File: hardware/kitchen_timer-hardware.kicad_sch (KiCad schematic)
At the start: 15 parts

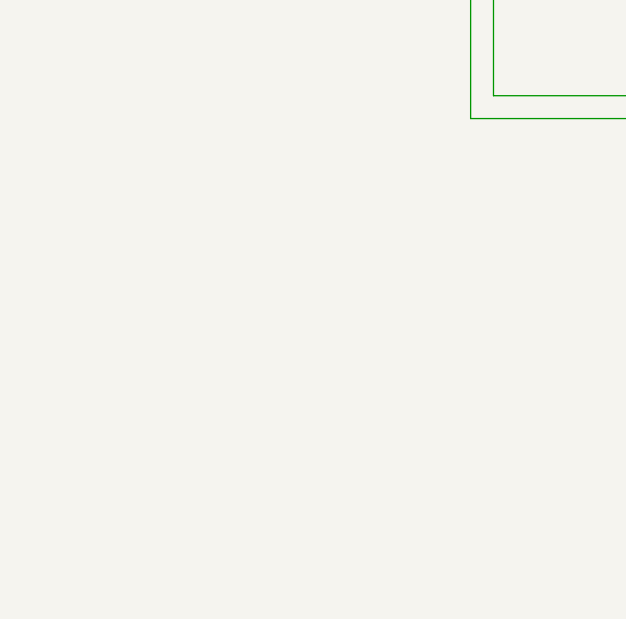
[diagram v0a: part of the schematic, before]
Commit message: Added mounting holes.
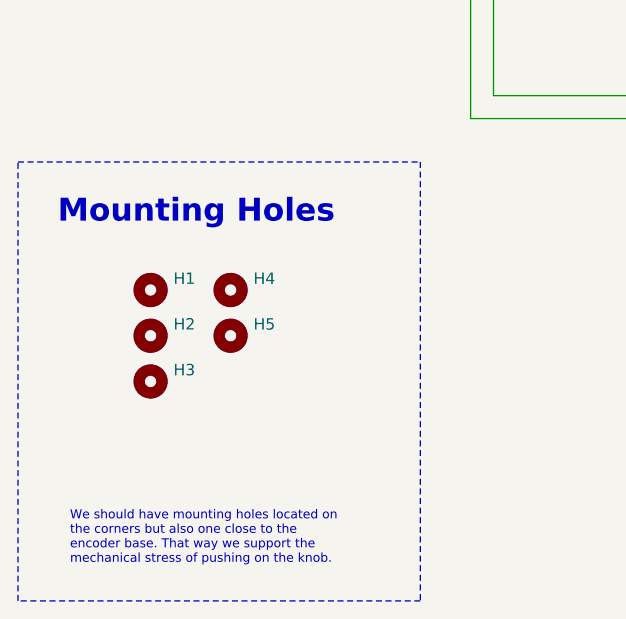
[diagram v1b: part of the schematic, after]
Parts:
- added H1, H2, H3, H4, H5: MountingHole, symbol Mechanical:MountingHole
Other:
- note added: "Mounting Holes"

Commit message: Electric Rules Check completed.
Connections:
- net ${VCC} Boost Converter/PP_GND is gone; now on net GND: TP11.1
- net BMS & Power Path/GND-USB is gone; now on net GND: TP15.1
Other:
- sheet ${VCC} Boost Converter ports: added none; removed PP_GND
- sheet BMS & Power Path ports: added GND; removed GND-USB, PP_GND
- sheet LED Matrices Display ports: added ${MAT1A}{DIG}, ${MAT1A}{SEG}, ${MAT1B}{DIG}, ${MAT1B}{SEG}, ${MAT2A}{DIG}, ${MAT2A}{SEG}, ${MAT2B}{DIG}, ${MAT2B}{SEG}; removed ${MAT1A}_DIG, ${MAT1A}_SEG, ${MAT1B}_DIG, ${MAT1B}_SEG, ${MAT2A}_DIG, ${MAT2A}_SEG, ${MAT2B}_DIG, ${MAT2B}_SEG
- sheet LED Matrices Drivers ports: added ${MAT1A}{DIG}, ${MAT1B}{DIG}, ${MAT1B}{SEG}, ${MAT2A}{DIG}, ${MAT2A}{SEG}, ${MAT2B}{DIG}, ${MAT2B}{SEG}, Mat1A{SEG}; removed ${MAT1A}_DIG, ${MAT1A}_SEG, ${MAT1B}_DIG, ${MAT1B}_SEG, ${MAT2A}_DIG, ${MAT2A}_SEG, ${MAT2B}_DIG, ${MAT2B}_SEG
- sheet USB-C & UART Debugger ports: added GND; removed GND-USB
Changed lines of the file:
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@@
 	)
 	(junction
-		(at 124.46 140.97)
-		(diameter 0)
-		(color 0 0 0 0)
-	)
-	(junction
 		(at 123.19 93.98)
 		(diameter 0)
@@
 	)
 	(junction
+		(at 124.46 140.97)
+		(diameter 0)
+		(color 0 0 0 0)
+	)
+	(junction
 		(at 123.19 88.9)
 		(diameter 0)
@@
 	(wire
 		(pts
+			(xy 124.46 140.97) (xy 128.27 140.97)
+		)
+		(stroke
+			(width 0)
+			(type default)
+		)
+	)
+	(wire
+		(pts
 			(xy 123.19 93.98) (xy 135.89 93.98)
 		)
@@
 		)
 	)
-	(wire
-		(pts
-			(xy 124.46 140.97) (xy 138.43 140.97)
-		)
-		(stroke
-			(width 0)
-			(type default)
-		)
-	)
 	(bus
 		(pts
@@
 	(wire
 		(pts
+			(xy 128.27 140.97) (xy 128.27 144.78)
+		)
+		(stroke
+			(width 0)
+			(type default)
+		)
+	)
+	(wire
+		(pts
 			(xy 55.88 68.58) (xy 55.88 67.31)
 		)
@@
 	(wire
 		(pts
-			(xy 66.04 71.12) (xy 66.04 140.97)
-		)
-		(stroke
-			(width 0)
-			(type default)
-		)
-	)
-	(wire
-		(pts
 			(xy 62.23 57.15) (xy 62.23 58.42)
 		)
@@
 	(wire
 		(pts
-			(xy 66.04 140.97) (xy 86.36 140.97)
-		)
-		(stroke
-			(width 0)
-			(type default)
-		)
-	)
-	(wire
-		(pts
-			(xy 55.88 71.12) (xy 66.04 71.12)
+			(xy 55.88 71.12) (xy 59.69 71.12)
 		)
 		(stroke
@@
 		)
 	)
+	(wire
+		(pts
+			(xy 59.69 71.12) (xy 59.69 74.93)
+		)
+		(stroke
+			(width 0)
+			(type default)
+		)
+	)
 	(bus
 		(pts
@@
 	(global_label "GND"
 		(shape output)
+		(at 59.69 74.93 0)
+		(fields_autoplaced yes)
+		(effects
+			(font
+				(size 1.27 1.27)
+			)
+			(justify left)
+		)
+		(property "Intersheetrefs" "${INTERSHEET_REFS}"
+			(at 66.5457 74.93 0)
+			(effects
+				(font
+					(size 1.27 1.27)
+				)
+				(justify left)
+				(hide yes)
+			)
+		)
+	)
+	(global_label "GND"
+		(shape output)
+		(at 128.27 144.78 0)
+		(fields_autoplaced yes)
+		(effects
+			(font
+				(size 1.27 1.27)
+			)
+			(justify left)
+		)
+		(property "Intersheetrefs" "${INTERSHEET_REFS}"
+			(at 135.1257 144.78 0)
+			(effects
+				(font
+					(size 1.27 1.27)
+				)
+				(justify left)
+				(hide yes)
+			)
+		)
+	)
+	(global_label "GND"
+		(shape output)
 		(at 186.69 140.97 0)
 		(fields_autoplaced yes)
@@
 			)
 		)
-		(pin "${MAT1A}_DIG" output
-			(at 218.44 53.34 0)
+		(pin "Mat1A{SEG}" output
+			(at 218.44 50.8 0)
 			(effects
 				(font
@@
 			)
 		)
-		(pin "${MAT1A}_SEG" output
-			(at 218.44 50.8 0)
+		(pin "${MAT1A}{DIG}" output
+			(at 218.44 53.34 0)
 			(effects
 				(font
@@
 			)
 		)
-		(pin "${MAT1B}_DIG" output
+		(pin "${MAT1B}{DIG}" output
 			(at 218.44 59.69 0)
 			(effects
@@
 			)
 		)
-		(pin "${MAT1B}_SEG" output
+		(pin "${MAT1B}{SEG}" output
 			(at 218.44 57.15 0)
 			(effects
@@
 			)
 		)
-		(pin "${MAT2A}_DIG" output
+		(pin "${MAT2A}{DIG}" output
 			(at 218.44 66.04 0)
 			(effects
@@
 			)
 		)
-		(pin "${MAT2A}_SEG" output
+		(pin "${MAT2A}{SEG}" output
 			(at 218.44 63.5 0)
 			(effects
@@
 			)
 		)
-		(pin "${MAT2B}_DIG" output
+		(pin "${MAT2B}{DIG}" output
 			(at 218.44 72.39 0)
 			(effects
@@
 			)
 		)
-		(pin "${MAT2B}_SEG" output
+		(pin "${MAT2B}{SEG}" output
 			(at 218.44 69.85 0)
 			(effects
@@
 			)
 		)
-		(pin "${MAT1A}_DIG" input
+		(pin "${MAT1A}{DIG}" input
 			(at 236.22 53.34 180)
 			(effects
@@
 			)
 		)
-		(pin "${MAT1A}_SEG" input
+		(pin "${MAT1A}{SEG}" input
 			(at 236.22 50.8 180)
 			(effects
@@
 			)
 		)
-		(pin "${MAT1B}_DIG" input
+		(pin "${MAT1B}{DIG}" input
 			(at 236.22 59.69 180)
 			(effects
@@
 			)
 		)
-		(pin "${MAT2A}_DIG" input
-			(at 236.22 66.04 180)
+		(pin "${MAT1B}{SEG}" input
+			(at 236.22 57.15 180)
 			(effects
 				(font
@@
 			)
 		)
-		(pin "${MAT2A}_SEG" input
-			(at 236.22 63.5 180)
+		(pin "${MAT2A}{DIG}" input
+			(at 236.22 66.04 180)
 			(effects
 				(font
@@
 			)
 		)
-		(pin "${MAT2B}_DIG" input
-			(at 236.22 72.39 180)
+		(pin "${MAT2A}{SEG}" input
+			(at 236.22 63.5 180)
 			(effects
 				(font
@@
 			)
 		)
-		(pin "${MAT2B}_SEG" input
-			(at 236.22 69.85 180)
+		(pin "${MAT2B}{DIG}" input
+			(at 236.22 72.39 180)
 			(effects
 				(font
@@
 			)
 		)
-		(pin "${MAT1B}_SEG" input
-			(at 236.22 57.15 180)
+		(pin "${MAT2B}{SEG}" input
+			(at 236.22 69.85 180)
 			(effects
 				(font
@@
 			)
 		)
-		(pin "PP_GND" input
-			(at 138.43 140.97 180)
-			(effects
-				(font
-					(size 1.27 1.27)
-				)
-				(justify left)
-			)
-		)
 		(pin "GND" output
 			(at 171.45 140.97 0)
@@
 			)
 		)
-		(pin "GND-USB" input
-			(at 86.36 140.97 180)
-			(effects
-				(font
-					(size 1.27 1.27)
-				)
-				(justify left)
-			)
-		)
 		(pin "+5V-USB" input
 			(at 86.36 138.43 180)
@@
 			)
 		)
-		(pin "PP_GND" output
+		(pin "GND" output
 			(at 119.38 140.97 0)
 			(effects
@@
 			)
 		)
-		(pin "GND-USB" output
-			(at 52.07 71.12 0)
+		(pin "CH340_RXD" input
+			(at 52.07 55.88 0)
 			(effects
 				(font
@@
 			)
 		)
-		(pin "CH340_RXD" input
-			(at 52.07 55.88 0)
+		(pin "­CH340_TXD" output
+			(at 52.07 53.34 0)
 			(effects
 				(font
@@
 			)
 		)
-		(pin "­CH340_TXD" output
-			(at 52.07 53.34 0)
+		(pin "GND" output
+			(at 52.07 71.12 0)
 			(effects
 				(font

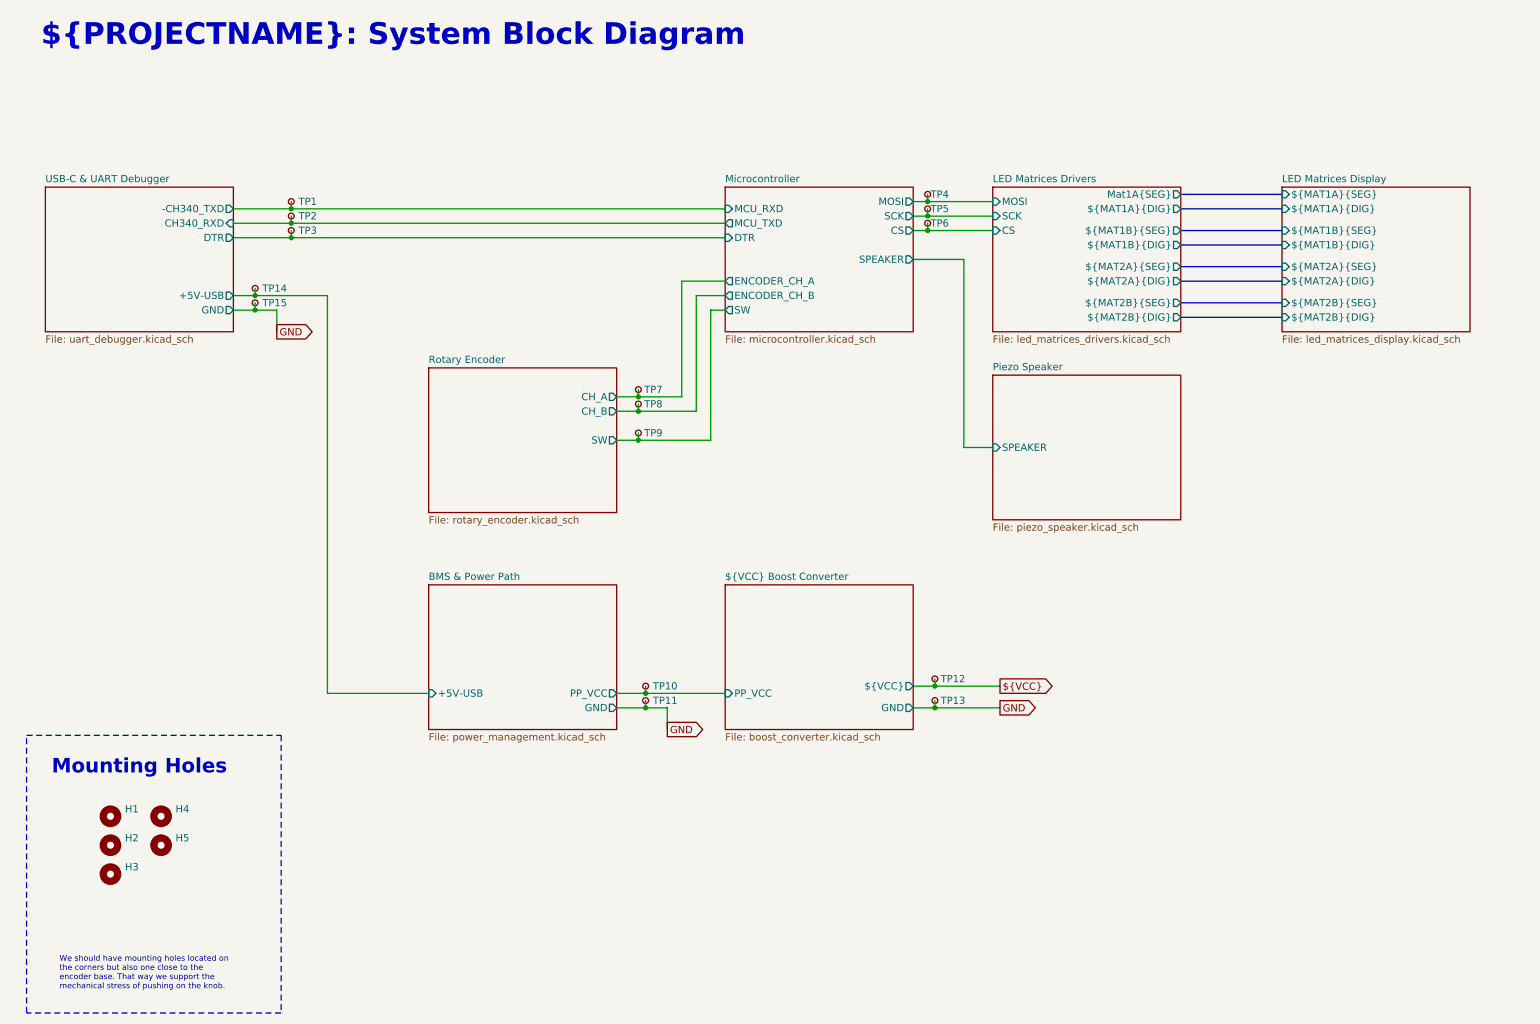
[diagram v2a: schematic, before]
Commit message: Added footprints to mounting holes and selected a part for the test LED.
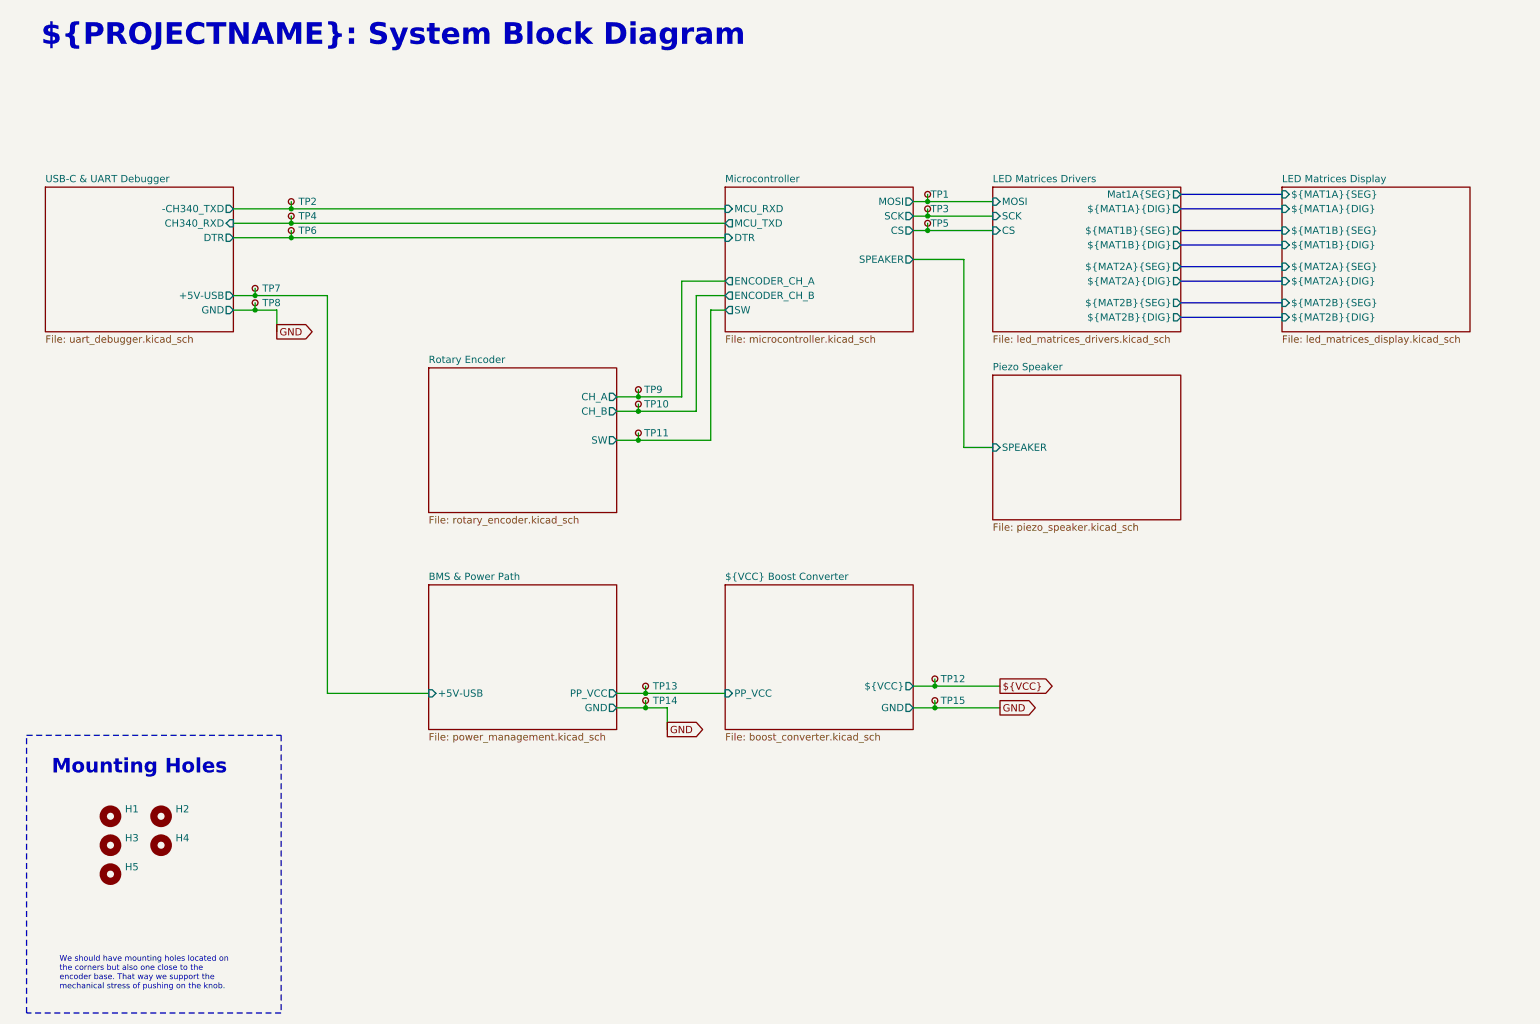
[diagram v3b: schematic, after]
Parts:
- H1: footprint (none) -> MountingHole:MountingHole_2.2mm_M2
- H2: renamed from H4; footprint (none) -> MountingHole:MountingHole_2.2mm_M2
- H3: renamed from H2; footprint (none) -> MountingHole:MountingHole_2.2mm_M2
- H4: renamed from H5; footprint (none) -> MountingHole:MountingHole_2.2mm_M2
- H5: renamed from H3; footprint (none) -> MountingHole:MountingHole_2.2mm_M2
- renumbered TP4 to TP1, TP8 to TP10, TP9 to TP11, TP10 to TP13, TP11 to TP14, TP13 to TP15, TP1 to TP2, TP5 to TP3, TP2 to TP4, TP6 to TP5, TP3 to TP6, TP14 to TP7, TP15 to TP8, TP7 to TP9

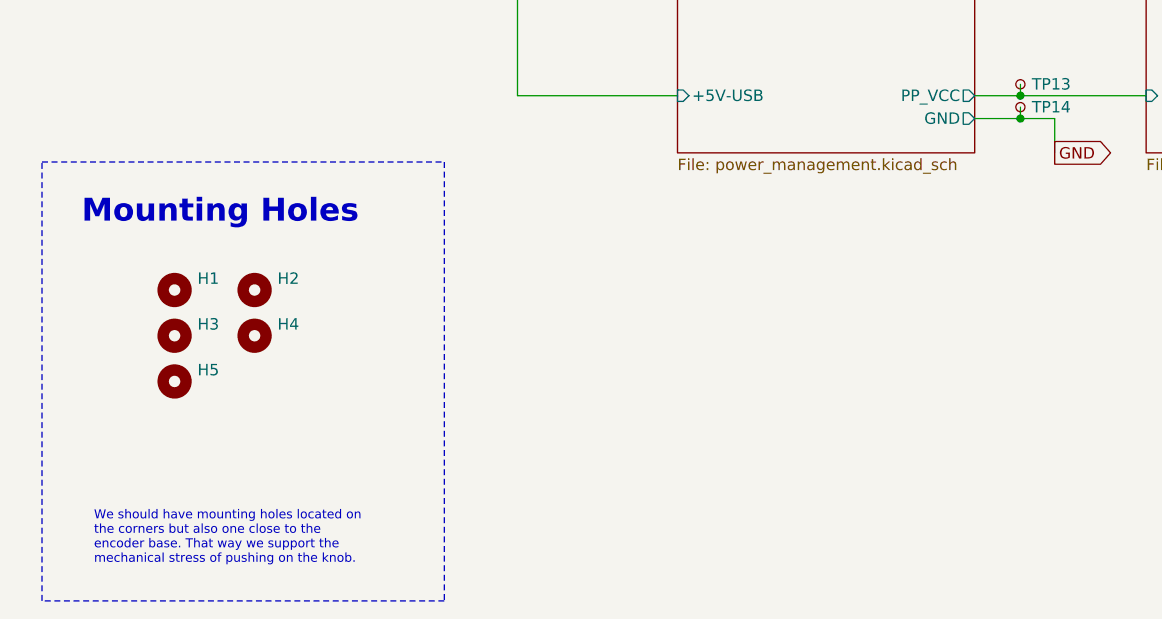
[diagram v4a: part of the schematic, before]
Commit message: Added the Enclosure Mounting Holes
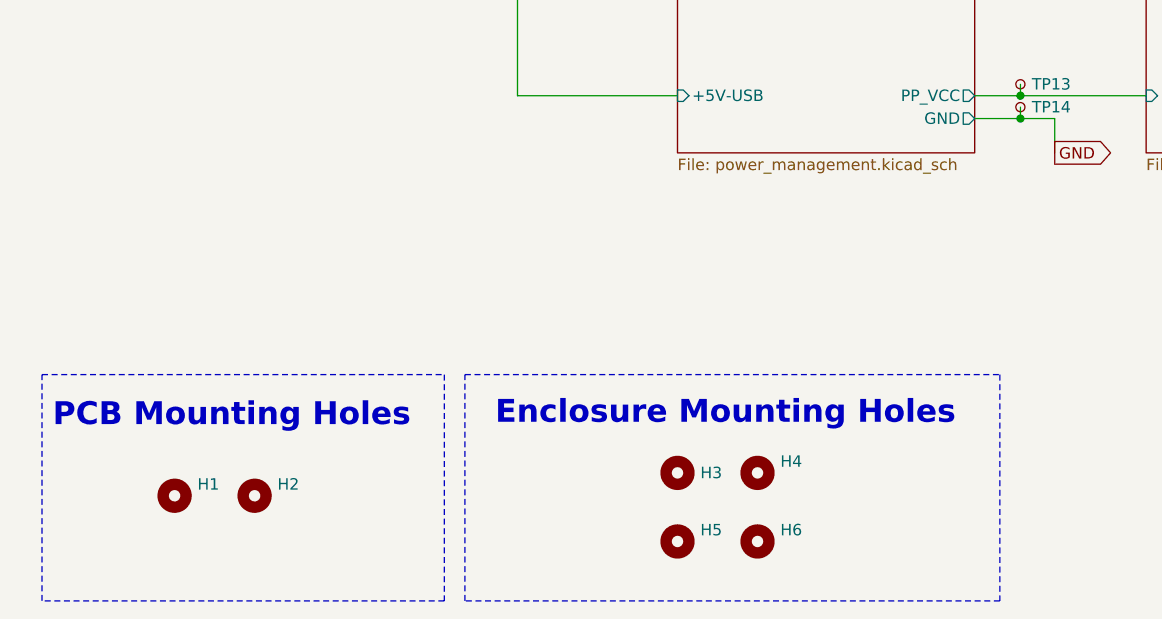
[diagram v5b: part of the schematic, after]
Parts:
- added H6: MountingHole, MountingHole:MountingHole_3.2mm_M3, symbol Mechanical:MountingHole
- H3, H4, H5: footprint MountingHole:MountingHole_2.2mm_M2 -> MountingHole:MountingHole_3.2mm_M3
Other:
- note added: "Enclosure Mounting Holes"
- note added: "PCB Mounting Holes"
- note removed: "Mounting Holes"
- moved on the sheet: H1, H2

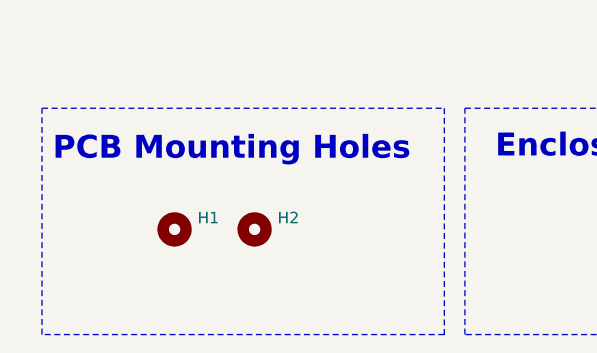
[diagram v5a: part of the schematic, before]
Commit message: Put the mounting holes in place and aligned components.
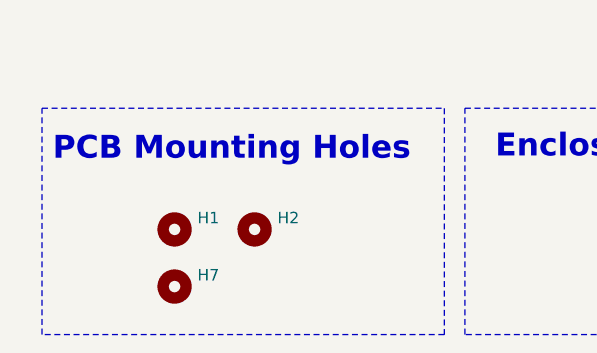
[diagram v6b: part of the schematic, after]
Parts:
- added H7: MountingHole, MountingHole:MountingHole_2.2mm_M2, symbol Mechanical:MountingHole
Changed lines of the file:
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@@
+	)
+	(symbol
+		(lib_id "Mechanical:MountingHole")
+		(at 30.48 189.23 0)
+		(unit 1)
+		(exclude_from_sim no)
+		(in_bom no)
+		(on_board yes)
+		(dnp no)
+		(fields_autoplaced yes)
+		(property "Reference" "H7"
+			(at 33.02 187.9599 0)
+			(effects
+				(font
+					(size 1.27 1.27)
+				)
+				(justify left)
+			)
+		)
+		(property "Value" "MountingHole"
+			(at 33.02 190.4999 0)
+			(effects
+				(font
+					(size 1.27 1.27)
+				)
+				(justify left)
+				(hide yes)
+			)
+		)
+		(property "Footprint" "MountingHole:MountingHole_2.2mm_M2"
+			(at 30.48 189.23 0)
+			(effects
+				(font
+					(size 1.27 1.27)
+				)
+				(hide yes)
+			)
+		)
+		(property "Datasheet" "~"
+			(at 30.48 189.23 0)
+			(effects
+				(font
+					(size 1.27 1.27)
+				)
+				(hide yes)
+			)
+		)
+		(property "Description" "Mounting Hole without connection"
+			(at 30.48 189.23 0)
+			(effects
+				(font
+					(size 1.27 1.27)
+				)
+				(hide yes)
+			)
+		)
+		(property "Supplier Unit Price" "~"
+			(at 30.48 189.23 0)
+			(effects
+				(font
+					(size 1.27 1.27)
+				)
+				(hide yes)
+			)
+		)
+		(property "Part Num" ""
+			(at 30.48 189.23 0)
+			(effects
+				(font
+					(size 1.27 1.27)
+				)
+				(hide yes)
+			)
+		)
+		(property "Package" "~"
+			(at 30.48 189.23 0)
+			(effects
+				(font
+					(size 1.27 1.27)
+				)
+				(hide yes)
+			)
+		)
+		(property "Manuf. Name" "~"
+			(at 30.48 189.23 0)
+			(effects
+				(font
+					(size 1.27 1.27)
+				)
+				(hide yes)
+			)
+		)
+		(property "Manuf. Part #" "~"
+			(at 30.48 189.23 0)
+			(effects
+				(font
+					(size 1.27 1.27)
+				)
+				(hide yes)
+			)
+		)
+		(property "Supplier Name" "~"
+			(at 30.48 189.23 0)
+			(effects
+				(font
+					(size 1.27 1.27)
+				)
+				(hide yes)
+			)
+		)
+		(property "Supplier Part #" "~"
+			(at 30.48 189.23 0)
+			(effects
+				(font
+					(size 1.27 1.27)
+				)
+				(hide yes)
+			)
+		)
+		(property "Supplier Link" "~"
+			(at 30.48 189.23 0)
+			(effects
+				(font
+					(size 1.27 1.27)
+				)
+				(hide yes)
+			)
+		)
+		(property "Manufacturer_Name" ""
+			(at 30.48 189.23 0)
+			(effects
+				(font
+					(size 1.27 1.27)
+				)
+				(hide yes)
+			)
+		)
+		(property "Manufacturer_Part_Number" ""
+			(at 30.48 189.23 0)
+			(effects
+				(font
+					(size 1.27 1.27)
+				)
+				(hide yes)
+			)
+		)
+		(property "Mouser Part Number" ""
+			(at 30.48 189.23 0)
+			(effects
+				(font
+					(size 1.27 1.27)
+				)
+				(hide yes)
+			)
+		)
+		(property "Mouser Price/Stock" ""
+			(at 30.48 189.23 0)
+			(effects
+				(font
+					(size 1.27 1.27)
+				)
+				(hide yes)
+			)
+		)
+		(instances
+			(project "kitchen_timer-hardware"
+				(path "/8963deea-96bc-4401-b671-98fbe9ed9c6a"
+					(reference "H7")
+					(unit 1)
+				)
+			)
+		)
 	)
 	(symbol
